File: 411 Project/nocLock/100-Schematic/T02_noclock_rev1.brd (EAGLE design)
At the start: 81.3 x 81.3 mm, 57 parts, among them J1 ICSP, J3 5BC-3-CA-F, J4 640455-2, J5 640455-2, J6 640455-2, J7 640455-2, J8 640455-2, Q1 DMN63D8LDW-7, Q3 DMG1012UW-7, U1 ATMEGA88A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

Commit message: Revised PCB layout.
Some work still needs to be done. Figure out a 5V power place rather
than a single trace to all things 5V.
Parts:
- moved TP5 21.6 mm to (33.0, 11.4)
- moved Q3 8.85 mm to (62.6, 34.1)
- moved D2 7.97 mm to (62.5, 21.5), flipped to the bottom, turned to 315 degrees
- moved C6 7.84 mm to (69.1, 34.2), turned to 180 degrees
- moved R10 7.55 mm to (71.6, 41.2), turned to 180 degrees
- moved TP1 5.81 mm to (56.4, 31.5)
- moved R6 5.29 mm to (69.1, 26.5)
- moved TP7 5.09 mm to (52.1, 59.4)
- moved TP10 5.04 mm to (25.4, 19.9)
- moved R11 2.53 mm to (66.4, 41.2), turned to 180 degrees
- moved D4 0.37 mm to (21.3, 21.6)
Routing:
- net +5V: track 239.5 -> 179.6 mm
- net GND: track 411.0 -> 358.4 mm, vias 21 -> 19
- net N$13: track 13.4 -> 6.53 mm, vias 2 -> 0
- net N$9: track 6.48 -> 12.6 mm
- net N$11: track 16.1 -> 12.0 mm
- net SCK: track 30.6 -> 32.3 mm
- net SOLENOID_CONTROL: track 20.8 -> 19.4 mm
- net N$10: track 23.7 -> 22.4 mm
- added copper zone on layer 1, net +5VD
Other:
- board text added: "ICSP"

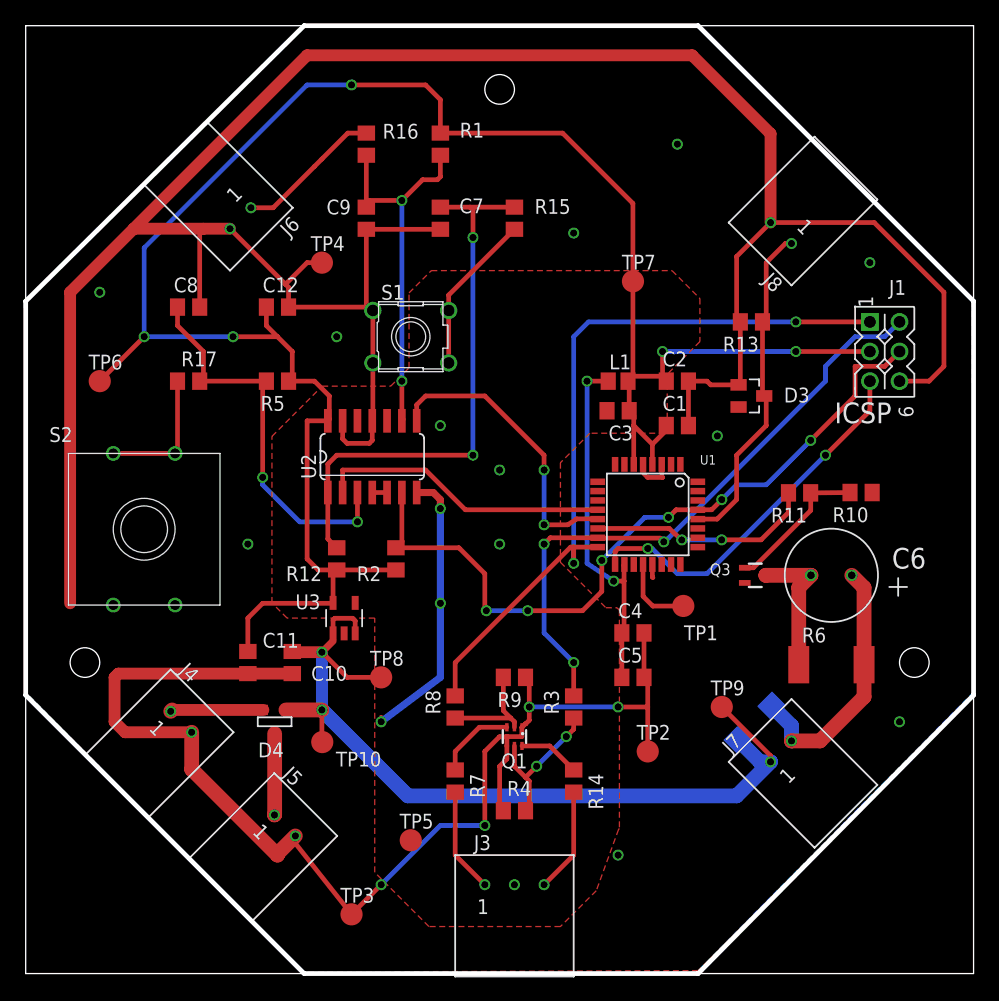
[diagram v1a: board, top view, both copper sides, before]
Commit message: Board revision
Fixed various issues with current layout, aded logo, and team name.
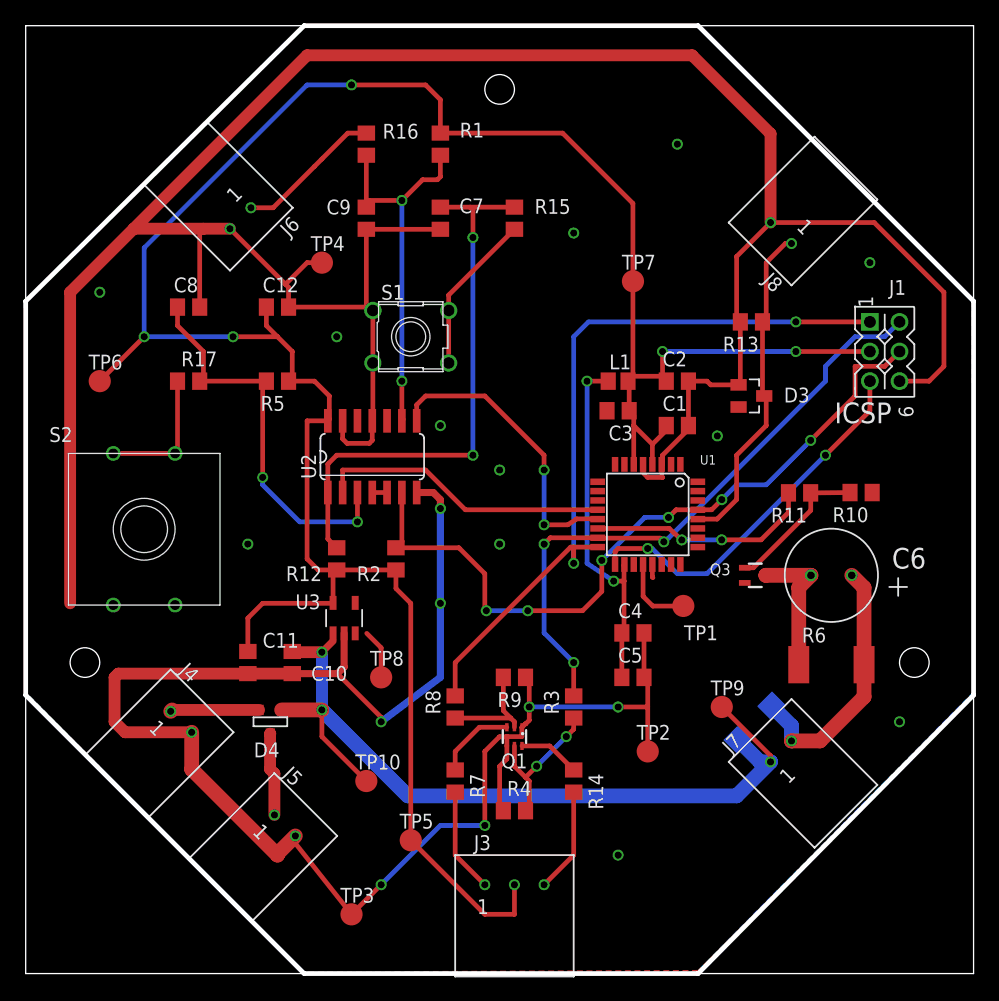
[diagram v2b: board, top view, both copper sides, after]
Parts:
- moved TP10 5.04 mm to (29.2, 16.5)
- moved D4 0.37 mm to (21.0, 21.6)
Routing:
- net +5V: track 179.6 -> 217.4 mm
- net GND: track 358.4 -> 375.6 mm
- net +9V: track 77.6 -> 77.0 mm
- removed copper zone on layer 1, net +5VD
